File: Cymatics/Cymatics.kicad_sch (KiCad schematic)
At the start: 75 parts, among them IC1 LMV358IDR, IC2 MAX7403CSA+, IC3 LMV358IDR, IC4 LMV358IDR, IC5 MAX7403CSA+, J1 Screw_Terminal_01x03, J10 Screw_Terminal_01x04, J11 Screw_Terminal_01x05, J12 Screw_Terminal_01x02, J13 Screw_Terminal_01x02, J14 RCU-0C, J15 Screw_Terminal_01x02, J16 Screw_Terminal_01x03, J17 Screw_Terminal_01x02, J18 Screw_Terminal_01x06, J19 RCU-0C, J2 Screw_Terminal_01x02, J20 RCU-0C, J21 RCU-0C, J22 RCU-0C, J23 RCU-0C, J24 RCU-0C, J3 Screw_Terminal_01x03, J4 Screw_Terminal_01x03, J5 Screw_Terminal_01x02, J6 Conn_01x16_Socket, J7 Conn_01x12_Socket, J8 Screw_Terminal_01x04, J9 Screw_Terminal_01x02, U1 SN74AHCT125DR, U2 MAX7480ESA+

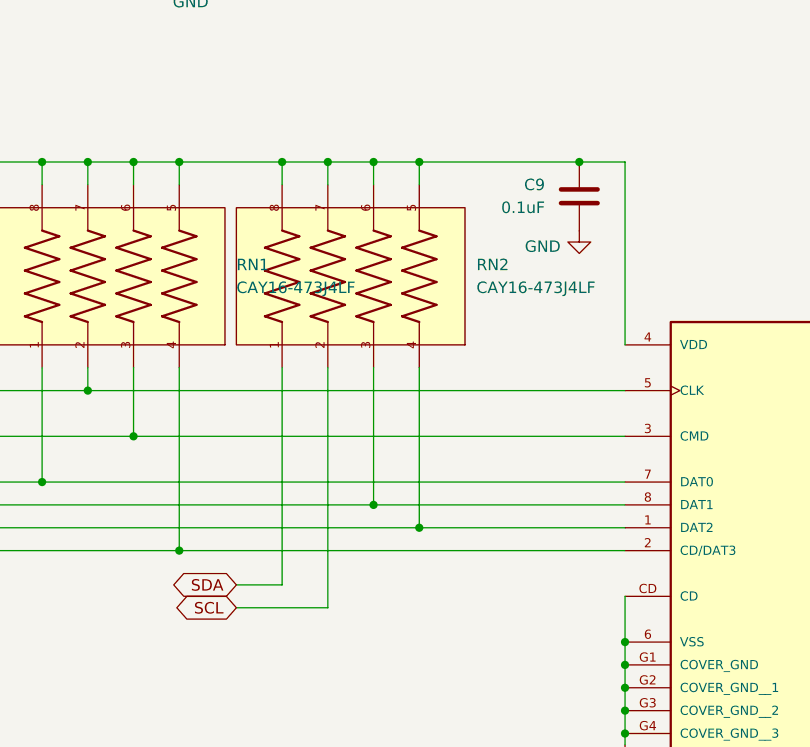
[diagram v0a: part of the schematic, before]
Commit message: use 10k pullup for I2C and DAT1/2
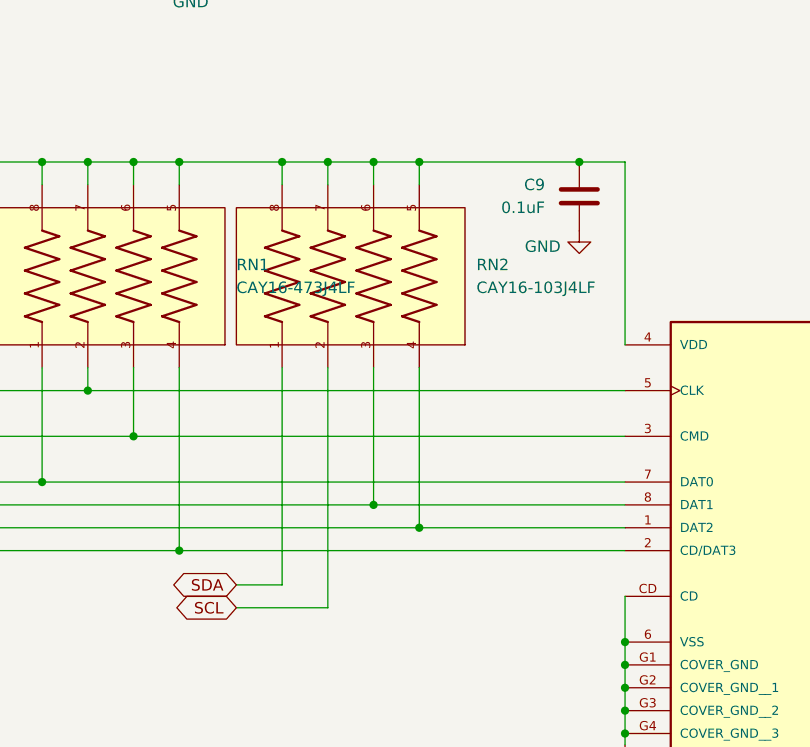
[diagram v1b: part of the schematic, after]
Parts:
- removed RN2: CAY16-473J4LF, CAY16:RESCAF80P320X160X60-8N, symbol CAY16:CAY16-473J4LF
- added RN2: CAY16-103J4LF, CAY16-103:RESCAF80P320X160X60-8N, symbol CAY16-103:CAY16-103J4LF
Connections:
- net 3V3: now also RN2.5, RN2.6, RN2.7, RN2.8
- net DAT1: now also RN2.3
- net DAT2: now also RN2.4
- net SCL: now also RN2.2
- net SDA: now also RN2.1

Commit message: Order for March PCB
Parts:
- C1, C10, C11, C15, C2, C6, C7, C8: In Stock 02-26-25 (none) -> 10; To Order 02-26-25 (none) -> 20
- C12, C13, C16, C18, C3, C4, C9: In Stock 02-26-25 (none) -> 8; To Order 02-26-25 (none) -> 20
- C14, C5, R10, R11, R14, R22, R23, R9: In Stock 02-26-25 (none) -> 5; To Order 02-26-25 (none) -> 10
- C17, J18, J6, J7, RN2, SD1, U1, U2: In Stock 02-26-25 (none) -> 0; To Order 02-26-25 (none) -> 3
- C19: In Stock 02-26-25 (none) -> 9; To Order 02-26-25 (none) -> 0
- IC1, IC3, IC4: In Stock 02-26-25 (none) -> 3; To Order 02-26-25 (none) -> 6
- IC2, IC5: In Stock 02-26-25 (none) -> 0; To Order 02-26-25 (none) -> 6
- J1, J16, J3, J4: In Stock 02-26-25 (none) -> 3; To Order 02-26-25 (none) -> 9
- J10, J11, J8: In Stock 02-26-25 (none) -> 1; To Order 02-26-25 (none) -> 2
- J12, J13, J15, J17, J2, J5, J9: In Stock 02-26-25 (none) -> 4; To Order 02-26-25 (none) -> 11
- J14, J19, J20, J21, J22, J23, J24: In Stock 02-26-25 (none) -> 3; To Order 02-26-25 (none) -> 18
- R1, R12, R13, R16, R17, R2, R20, R21, R24, R25, R3, R4, R7, R8: In Stock 02-26-25 (none) -> 4; To Order 02-26-25 (none) -> 50
- R5, R6: In Stock 02-26-25 (none) -> 6; To Order 02-26-25 (none) -> 0
- RN1: footprint CAY16:RESCAF80P320X160X60-8N -> CAY16-473:RESCAF80P320X160X60-8N; In Stock 02-26-25 (none) -> 0; To Order 02-26-25 (none) -> 3

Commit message: All changes up through Week 9, including making the step file
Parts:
- removed RN2: CAY16-103J4LF, CAY16-103:RESCAF80P320X160X60-8N, symbol CAY16-103:CAY16-103J4LF
- added C20: 10uF, Capacitor_SMD:C_0805_2012Metric, symbol Device:C
- added RN2: CAY16-473J4LF, CAY16-473:RESCAF80P320X160X60-8N, symbol CAY16:CAY16-473J4LF
- added RN3: CAY16-103J4LF, CAY16-103:RESCAF80P320X160X60-8N, symbol CAY16-103:CAY16-103J4LF
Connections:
- net 3V3: now also C20.1, RN2.6, RN2.7, RN2.8, RN3.7, RN3.8
- net DAT1: now also RN2.2
- net DAT2: now also RN2.1
- net GND: now also C20.2; no longer SD1.CD
- net SCL: now also RN3.2
- net SDA: now also RN3.1
- new net CD: RN2.3, SD1.CD
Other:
- note added: "1 -> BAT 2 -> EN 3 -> USB 4 -> 13, red LED 5 -> 12, internal pull-down resistor 6 -> 27 7 -> 33, 32 KHz crystal 8 -> 15 9 -> 32, 32 KHz crystal 10 -> 14 11 -> SCL 12 -> SDA"
- note removed: "1 -> BAT 2 -> EN 3 -> USB 4 -> 13, red LED 5 -> 12, internal pull-down resistor (DO NOT USE) 6 -> 27 7 -> 33, 32 KHz crystal 8 -> 15 9 -> 32, 32 KHz crystal 10 -> 14 11 -> SCL 12 -> SDA"
- moved on the sheet: C9, J1, J11, J18, J6, J7, J8, RN1

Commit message: added passive DAC filters to schem and layout
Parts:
- added C21, C22, C23: 10uF, Capacitor_SMD:C_0805_2012Metric, symbol Device:C
- added C24, C25: 0.1uF, Capacitor_SMD:C_0805_2012Metric, symbol Device:C
- added R15, R18: 1.5k, Resistor_SMD:R_1206_3216Metric, symbol Device:R
- added R19, R26: 3.3k, Resistor_SMD:R_1206_3216Metric, symbol Device:R
- RN3: In Stock 02-26-25 (none) -> 0
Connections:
- net A0: now also C21.2; no longer J12.2 (Pin_2)
- net A1: now also C22.2; no longer J13.2 (Pin_2)
- net BASS_OUT: now also C23.2; no longer J17.2 (Pin_2)
- net GND: now also C24.1, C25.1, R15.1, R18.1
- new net: C22.1, R18.2, R26.2
- new net: C25.2, J13.2 (Pin_2), R26.1
- new net: C21.1, R15.2, R19.2
- new net: C24.2, J12.2 (Pin_2), R19.1
- new net: C23.1, J17.2 (Pin_2)
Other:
- moved on the sheet: C1, C10, C11, C12, C13, C14, C15, C16, C17, C18, C19, C2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

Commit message: misc updates
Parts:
- C1, C10, C11, C15, C2, C20, C21, C22, C23, C6, C7, C8: In Stock 03-12-25 (none) -> 42; In Stock 03-20-25 (none) -> 37; In Stock 03-21-25 (none) -> 28; In Stock 03-28-25 (none) -> 38; To Order 03-21-25 (none) -> 8
- C12, C13, C16, C18, C24, C25, C3, C4, C9: In Stock 03-12-25 (none) -> 30; In Stock 03-20-25 (none) -> 27; In Stock 03-21-25 (none) -> 20; In Stock 03-28-25 (none) -> 30; To Order 03-21-25 (none) -> 7
- C14, C5, R10, R11, R14, R22, R23, R9: In Stock 03-12-25 (none) -> 15; In Stock 03-20-25 (none) -> 13; In Stock 03-21-25 (none) -> 11; In Stock 03-28-25 (none) -> 11; To Order 03-21-25 (none) -> 0
- C17, J6, J7, SD1, U1: In Stock 03-12-25 (none) -> 3; In Stock 03-20-25 (none) -> 2; In Stock 03-21-25 (none) -> 1; In Stock 03-28-25 (none) -> 3; To Order 03-21-25 (none) -> 2
- C19: In Stock 03-12-25 (none) -> 9; In Stock 03-20-25 (none) -> 8; In Stock 03-21-25 (none) -> 7; In Stock 03-28-25 (none) -> 7; To Order 03-21-25 (none) -> 0
- IC1, IC3, IC4: In Stock 03-12-25 (none) -> 13; In Stock 03-20-25 (none) -> 10; In Stock 03-21-25 (none) -> 7; In Stock 03-28-25 (none) -> 9; To Order 03-21-25 (none) -> 2
- IC2, IC5: In Stock 03-12-25 (none) -> 4; In Stock 03-20-25 (none) -> 2; In Stock 03-21-25 (none) -> 0; In Stock 03-28-25 (none) -> 6; To Order 03-21-25 (none) -> 6
- J1, J16, J3, J4: In Stock 03-12-25 (none) -> 2; In Stock 03-20-25 (none) -> 1; In Stock 03-21-25 (none) -> 0; In Stock 03-28-25 (none) -> 12; To Order 03-21-25 (none) -> 12
- J10, J8: In Stock 03-12-25 (none) -> 0; In Stock 03-20-25 (none) -> 0; In Stock 03-21-25 (none) -> 0; In Stock 03-28-25 (none) -> 6; To Order 03-21-25 (none) -> 6
- J11: In Stock 03-12-25 (none) -> 1; In Stock 03-20-25 (none) -> 1; In Stock 03-21-25 (none) -> 1; In Stock 03-28-25 (none) -> 3; To Order 03-21-25 (none) -> 2
- J12, J13, J15, J17, J2, J5, J9: In Stock 03-12-25 (none) -> 5; In Stock 03-20-25 (none) -> 5; In Stock 03-21-25 (none) -> 0; In Stock 03-28-25 (none) -> 21; To Order 03-21-25 (none) -> 21
- J14, J19, J20, J21, J22, J23, J24: In Stock 03-12-25 (none) -> 23; In Stock 03-20-25 (none) -> 16; In Stock 03-21-25 (none) -> 9; In Stock 03-28-25 (none) -> 21; To Order 03-21-25 (none) -> 12
- J18: In Stock 03-12-25 (none) -> 0; In Stock 03-20-25 (none) -> 0; In Stock 03-21-25 (none) -> 0; In Stock 03-28-25 (none) -> 3; To Order 03-21-25 (none) -> 3
- R1, R12, R13, R16, R17, R2, R20, R21, R24, R25, R3, R4, R7, R8: In Stock 03-12-25 (none) -> 54; In Stock 03-20-25 (none) -> 40; In Stock 03-21-25 (none) -> 26; In Stock 03-28-25 (none) -> 46; To Order 03-21-25 (none) -> 16
- R15, R18, R19, R26: In Stock 03-12-25 (none) -> 0; In Stock 03-20-25 (none) -> 2; In Stock 03-21-25 (none) -> 2; In Stock 03-28-25 (none) -> 12; To Order 03-21-25 (none) -> 4
- R5, R6: In Stock 03-12-25 (none) -> 6; In Stock 03-20-25 (none) -> 5; In Stock 03-21-25 (none) -> 4; In Stock 03-28-25 (none) -> 4; To Order 03-21-25 (none) -> 0
- RN1, RN2: In Stock 03-12-25 (none) -> 10; In Stock 03-20-25 (none) -> 8; In Stock 03-21-25 (none) -> 6; In Stock 03-28-25 (none) -> 6; To Order 03-21-25 (none) -> 0
- RN3: In Stock 03-12-25 (none) -> 10; In Stock 03-20-25 (none) -> 10; In Stock 03-21-25 (none) -> 8; In Stock 03-28-25 (none) -> 9; To Order 03-21-25 (none) -> 0
- U2: In Stock 03-12-25 (none) -> 2; In Stock 03-20-25 (none) -> 1; In Stock 03-21-25 (none) -> 0; In Stock 03-28-25 (none) -> 3; To Order 03-21-25 (none) -> 3
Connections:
- net SCL: now also RN3.1; no longer RN3.2
- net SDA: now also RN3.2; no longer RN3.1
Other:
- title: (none) -> Cymatics PCB
- moved on the sheet: C1, C10, C11, C12, C13, C14, C15, C16, C17, C18, C19, C2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
